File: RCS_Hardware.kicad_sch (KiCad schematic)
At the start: 39 parts, among them J1 SWD, J2 TYPE-C-31-M-12, U1 STM32F401CCU6, U2 AMS1117-3.3, U3 BMP280, U4 BNO055, Y1 16MHz, Y2 32.768Mhz

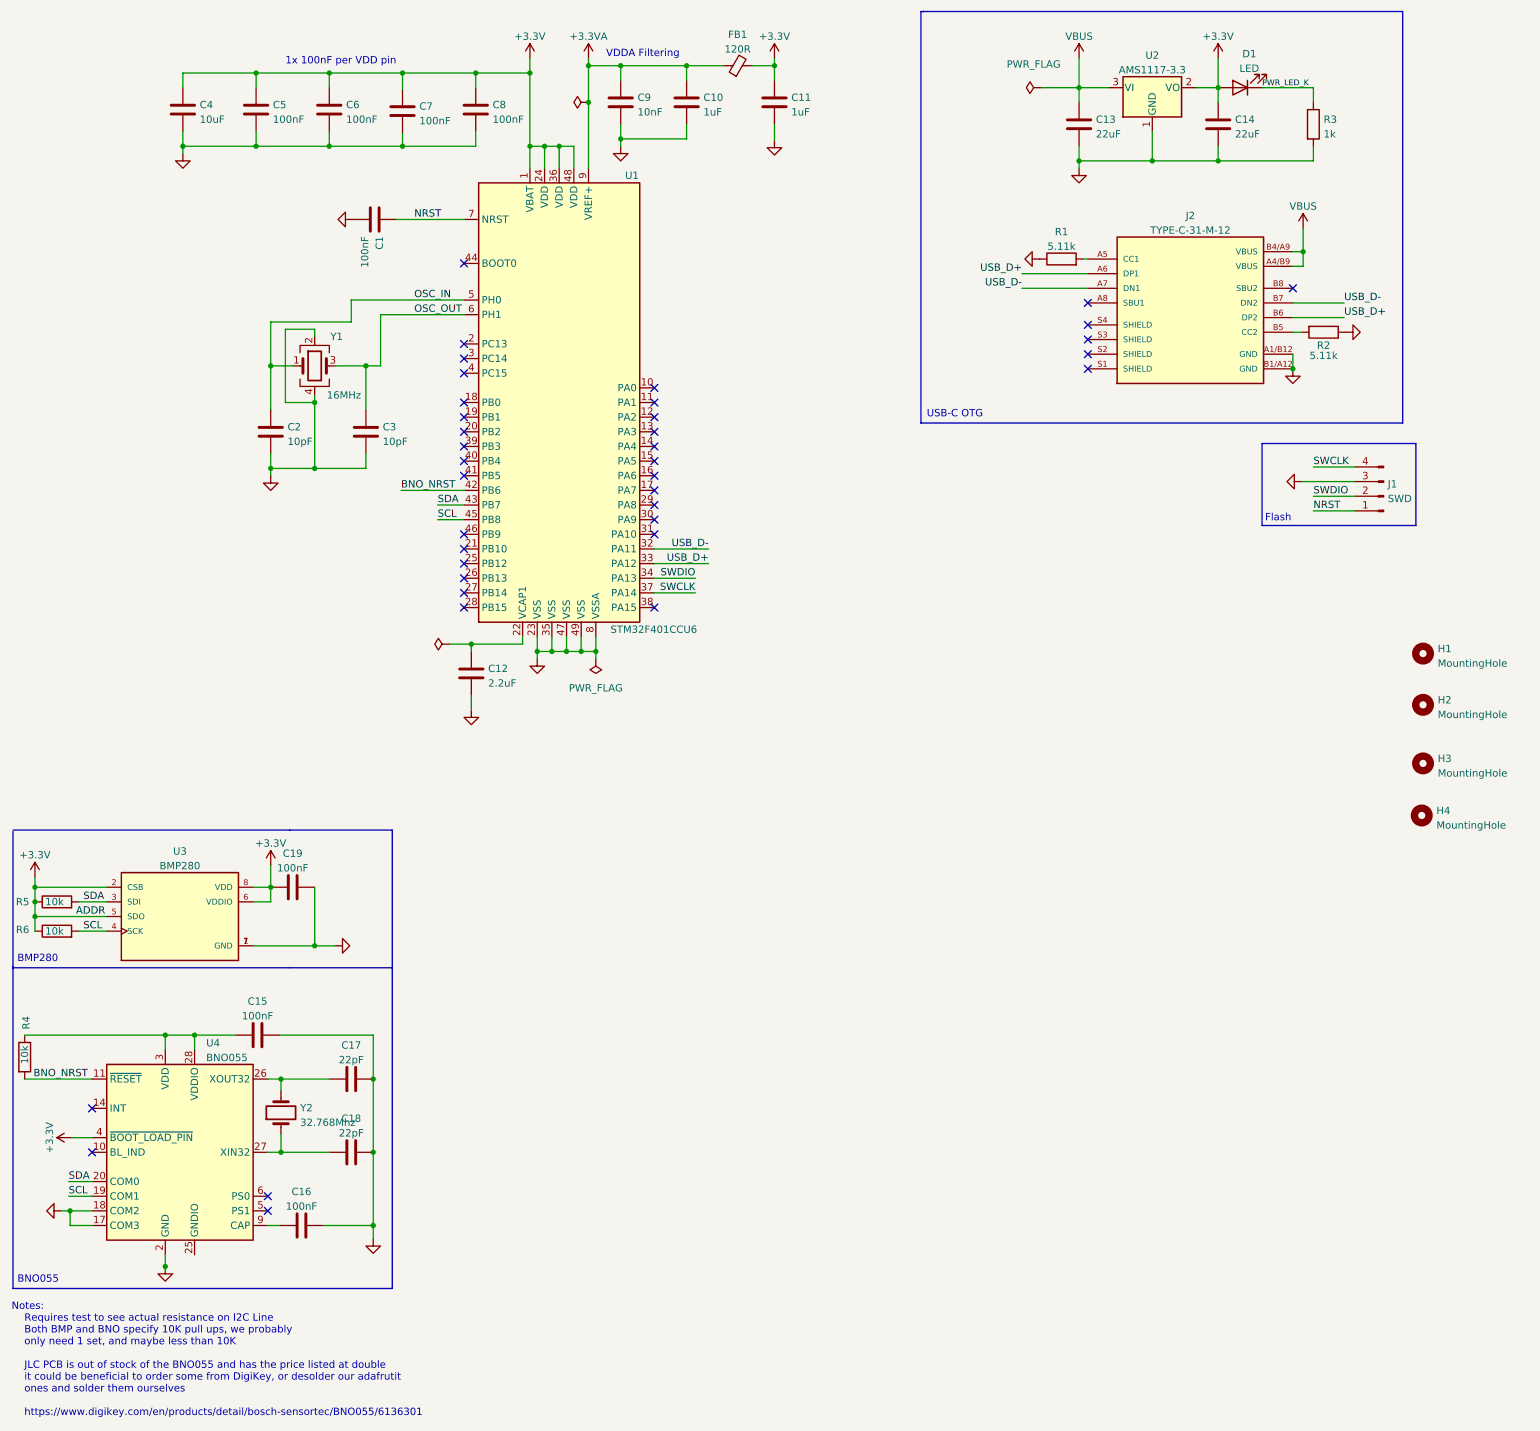
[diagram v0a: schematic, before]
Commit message: added SPI NOR flash chip fixed minor issues with BNO055 schema completed a rough layout of the entire current pcb
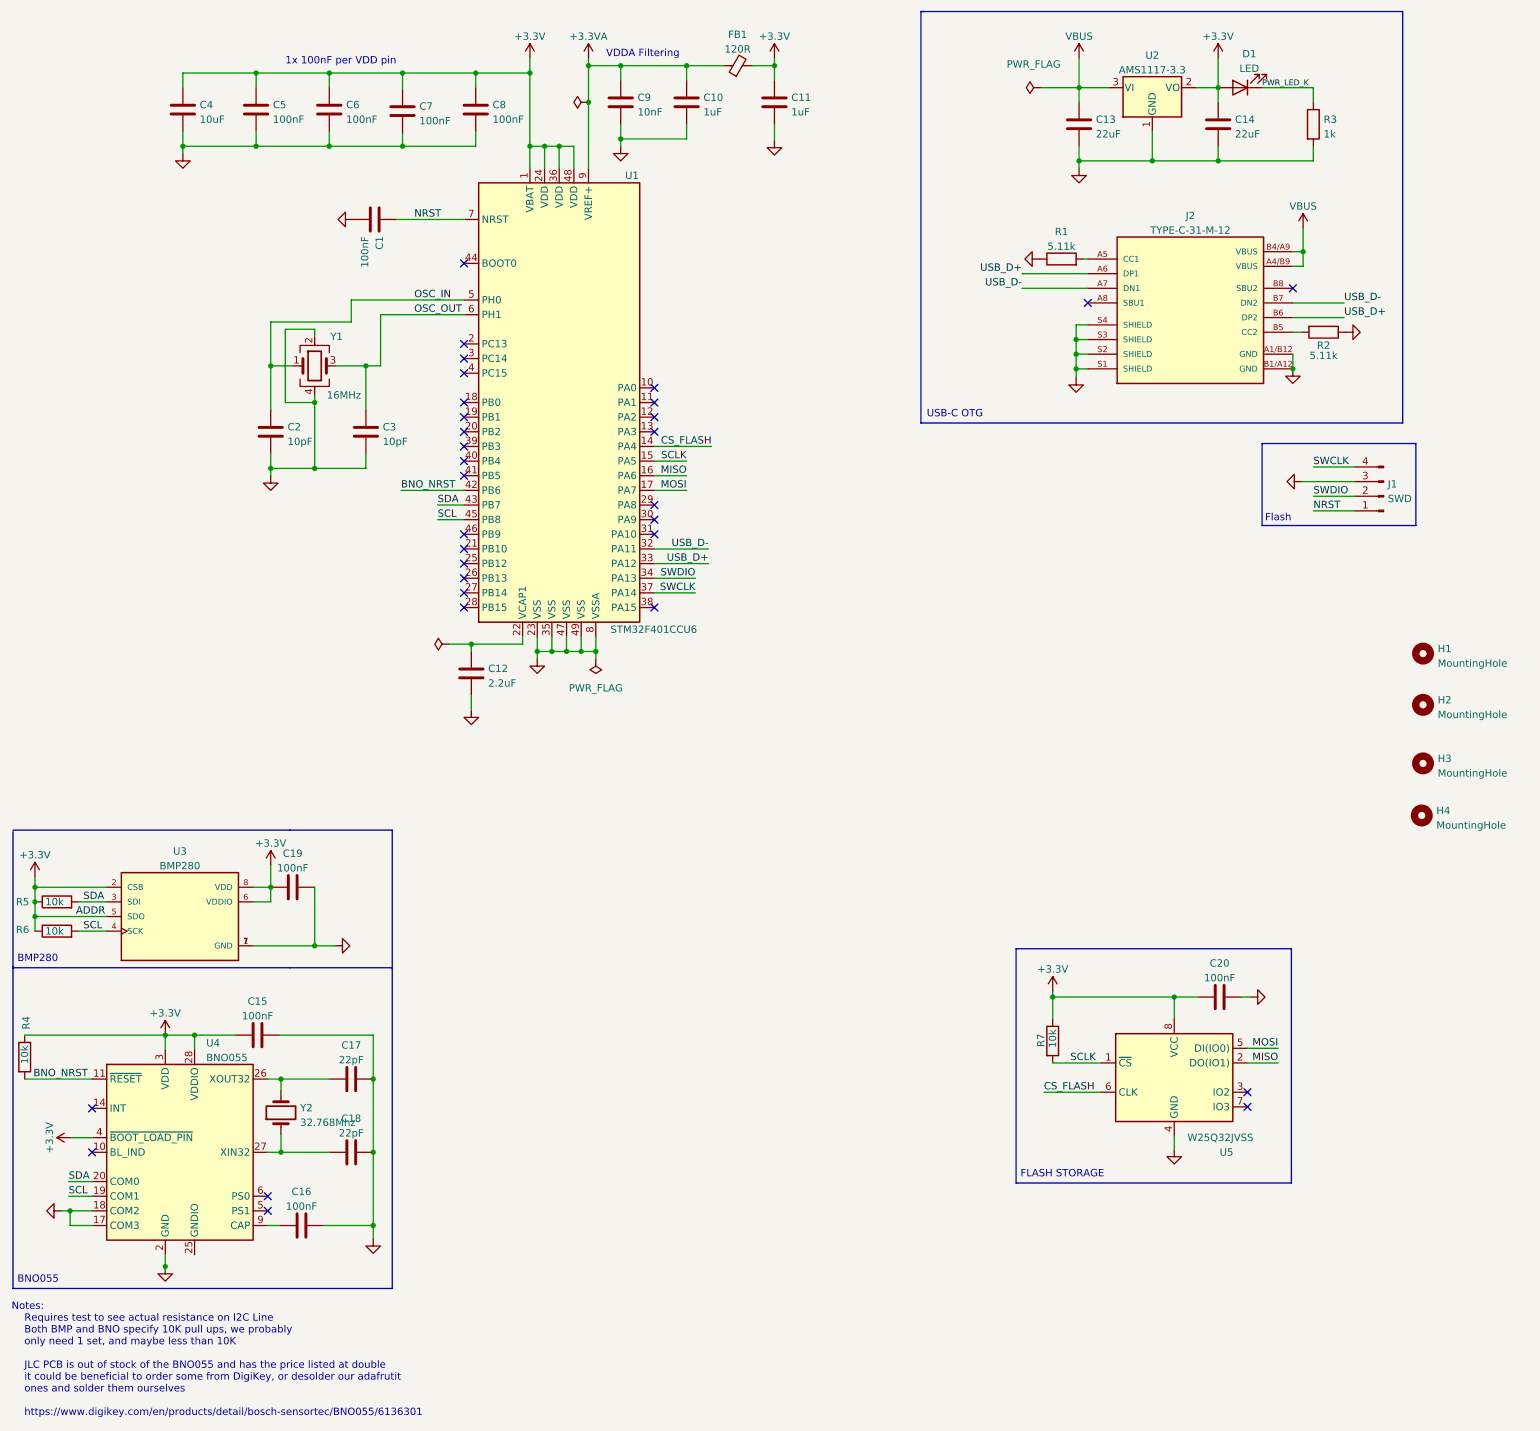
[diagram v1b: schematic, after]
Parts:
- added C20: 100nF, Capacitor_SMD:C_0402_1005Metric, symbol Device:C
- added R7: 10k, Resistor_SMD:R_0402_1005Metric, symbol Device:R
- added U5: W25Q32JVSS, Package_SO:SOIC-8_5.23x5.23mm_P1.27mm, symbol Memory_Flash:W25Q32JVSS
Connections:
- net +3.3V: now also C15.1, R4.1, U4.28 (VDDIO), U4.3 (VDD), C20.1, R7.1, U5.8 (VCC)
- net GND: now also J2.S1 (SHIELD), J2.S2 (SHIELD), J2.S3 (SHIELD), J2.S4 (SHIELD), C20.2, U5.4 (GND)
- net CS_FLASH: now reaches U1.14 (PA4)
- net CS_FLASH: now also U5.6 (CLK)
- net SCLK: now reaches U1.15 (PA5)
- net SCLK: now also R7.2, U5.1 (~{CS})
- net MISO: now reaches U1.16 (PA6)
- net MISO: now also U5.2 (DO(IO1))
- net MOSI: now reaches U1.17 (PA7)
- net MOSI: now also U5.5 (DI(IO0))
- no-connect marks 38 -> 32
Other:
- note added: "FLASH STORAGE"
